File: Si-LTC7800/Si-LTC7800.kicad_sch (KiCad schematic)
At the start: 40 parts, among them Q1 BSC100N06LS3_G, Q2 BSC100N06LS3_G, U1 LTC7800HUDC_PBF

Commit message: power traces sortof done
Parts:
- renumbered R3 to RSENSE
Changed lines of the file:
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@@
 		(on_board yes)
 		(dnp no)
-		(property "Reference" "R3"
+		(property "Reference" "RSENSE"
 			(at 217.17 94.742 90)
 			(effects
@@
 			(project "Si-LTC7800"
 				(path "/1cd71796-7ea7-422d-abea-f4fbd11d4a75"
-					(reference "R3")
+					(reference "RSENSE")
 					(unit 1)
 				)

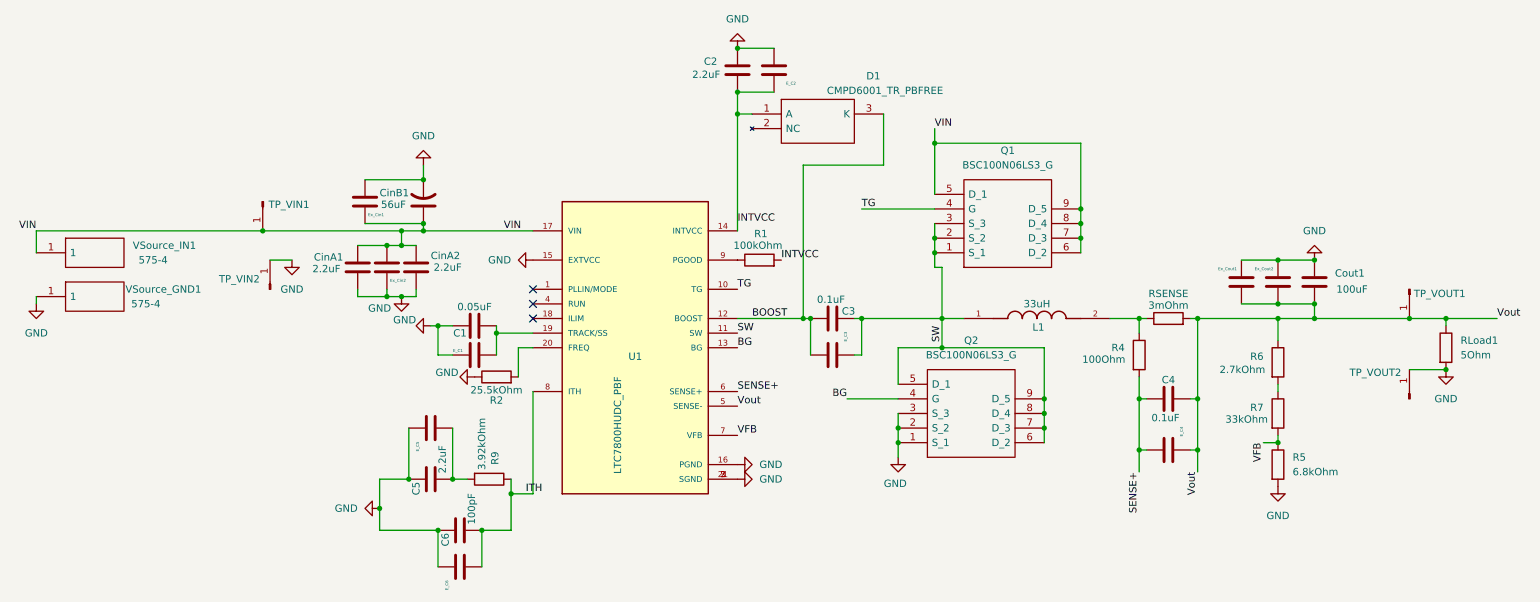
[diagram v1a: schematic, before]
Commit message: Changed font size and names on PCB
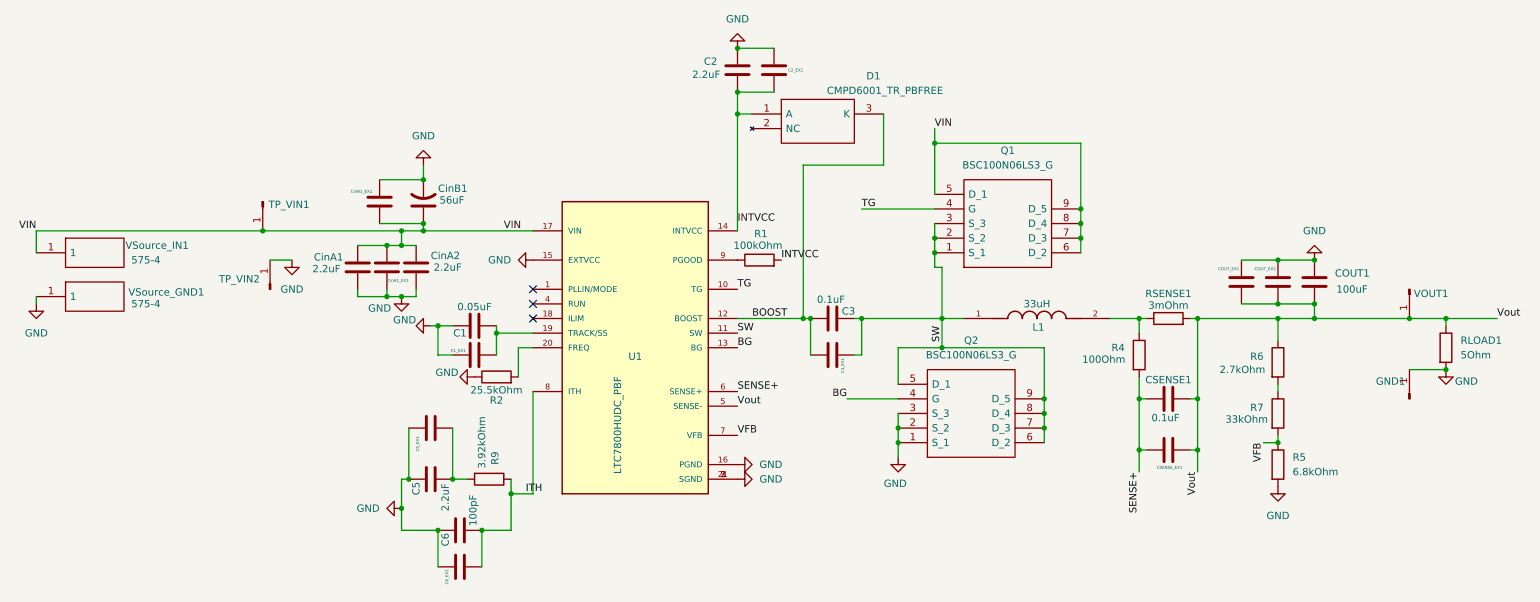
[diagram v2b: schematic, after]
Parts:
- renumbered E_C1 to C1_EX1, E_C2 to C2_EX1, E_C3 to C3_EX1, E_C5 to C5_EX1, E_C6 to C6_EX1, Cout1 to COUT1, Ex_Cout1 to COUT_EX1, Ex_Cout2 to COUT_EX2, C4 to CSENSE1, E_C4 to CSENSE_EX1, Ex_Cin2 to CinA1_EX1, Ex_Cin1 to CinB1_EX1, TP_VOUT2 to GND1, RLoad1 to RLOAD1, RSENSE to RSENSE1, TP_VOUT1 to VOUT1
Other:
- moved on the sheet: CinB1_EX1
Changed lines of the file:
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@@
 	)
 	(junction
-		(at 80.01 132.08)
+		(at 83.82 132.08)
 		(diameter 0)
 		(color 0 0 0 0)
@@
 	(wire
 		(pts
-			(xy 80.01 127) (xy 85.09 127)
+			(xy 83.82 127) (xy 85.09 127)
 		)
 		(stroke
@@
 	(wire
 		(pts
-			(xy 80.01 132.08) (xy 80.01 127)
+			(xy 83.82 132.08) (xy 83.82 127)
 		)
 		(stroke
@@
 	(wire
 		(pts
-			(xy 77.47 74.93) (xy 87.63 74.93)
+			(xy 80.01 74.93) (xy 87.63 74.93)
 		)
 		(stroke
@@
 	(wire
 		(pts
-			(xy 80.01 132.08) (xy 80.01 135.89)
+			(xy 83.82 132.08) (xy 83.82 135.89)
 		)
 		(stroke
@@
 	(wire
 		(pts
-			(xy 80.01 135.89) (xy 90.17 135.89)
+			(xy 83.82 135.89) (xy 90.17 135.89)
 		)
 		(stroke
@@
 	(wire
 		(pts
-			(xy 77.47 82.55) (xy 87.63 82.55)
+			(xy 80.01 82.55) (xy 87.63 82.55)
 		)
 		(stroke
@@
 		(on_board yes)
 		(dnp no)
-		(property "Reference" "E_C5"
+		(property "Reference" "C5_EX1"
 			(at 86.614 122.174 0)
 			(effects
@@
 			(project "Si-LTC7800"
 				(path "/1cd71796-7ea7-422d-abea-f4fbd11d4a75"
-					(reference "E_C5")
+					(reference "C5_EX1")
 					(unit 1)
 				)
@@
 		(on_board yes)
 		(dnp no)
-		(property "Reference" "E_C1"
-			(at 94.488 104.648 90)
+		(property "Reference" "C1_EX1"
+			(at 94.996 104.648 90)
 			(effects
 				(font
@@
 			(project "Si-LTC7800"
 				(path "/1cd71796-7ea7-422d-abea-f4fbd11d4a75"
-					(reference "E_C1")
+					(reference "C1_EX1")
 					(unit 1)
 				)
@@
 		(on_board yes)
 		(dnp no)
-		(property "Reference" "TP_VOUT2"
-			(at 248.666 108.458 90)
+		(property "Reference" "GND1"
+			(at 253.238 109.982 90)
 			(effects
 				(font
@@
 		)
 		(property "Value" "~"
-			(at 248.92 110.744 90)
+			(at 256.032 111.506 90)
 			(effects
 				(font
@@
 			(project "Si-LTC7800"
 				(path "/1cd71796-7ea7-422d-abea-f4fbd11d4a75"
-					(reference "TP_VOUT2")
+					(reference "GND1")
 					(unit 1)
 				)
@@
 		(on_board yes)
 		(dnp no)
-		(property "Reference" "TP_VOUT1"
+		(property "Reference" "VOUT1"
 			(at 259.842 94.742 90)
 			(effects
@@
 			(project "Si-LTC7800"
 				(path "/1cd71796-7ea7-422d-abea-f4fbd11d4a75"
-					(reference "TP_VOUT1")
+					(reference "VOUT1")
 					(unit 1)
 				)
@@
 		(on_board yes)
 		(dnp no)
-		(property "Reference" "Ex_Cin2"
-			(at 84.582 92.456 0)
+		(property "Reference" "CinA1_EX1"
+			(at 85.09 92.456 0)
 			(effects
 				(font
@@
 			(project "Si-LTC7800"
 				(path "/1cd71796-7ea7-422d-abea-f4fbd11d4a75"
-					(reference "Ex_Cin2")
+					(reference "CinA1_EX1")
 					(unit 1)
 				)
@@
 		(on_board yes)
 		(dnp no)
-		(property "Reference" "RSENSE"
+		(property "Reference" "RSENSE1"
 			(at 217.17 94.742 90)
 			(effects
@@
 			(project "Si-LTC7800"
 				(path "/1cd71796-7ea7-422d-abea-f4fbd11d4a75"
-					(reference "RSENSE")
+					(reference "RSENSE1")
 					(unit 1)
 				)
@@
 		(on_board yes)
 		(dnp no)
-		(property "Reference" "Cout1"
+		(property "Reference" "COUT1"
 			(at 246.126 91.186 0)
 			(effects
@@
 			(project "Si-LTC7800"
 				(path "/1cd71796-7ea7-422d-abea-f4fbd11d4a75"
-					(reference "Cout1")
+					(reference "COUT1")
 					(unit 1)
 				)
@@
 		(on_board yes)
 		(dnp no)
-		(property "Reference" "E_C2"
-			(at 152.4 58.166 0)
+		(property "Reference" "C2_EX1"
+			(at 153.67 55.88 0)
 			(effects
 				(font
@@
 		)
 		(property "Value" "~"
-			(at 150.368 57.404 0)
+			(at 152.908 56.642 0)
 			(effects
 				(font
@@
 			(project "Si-LTC7800"
 				(path "/1cd71796-7ea7-422d-abea-f4fbd11d4a75"
-					(reference "E_C2")
+					(reference "C2_EX1")
 					(unit 1)
 				)
@@
 		(on_board yes)
 		(dnp no)
-		(property "Reference" "E_C4"
-			(at 219.456 117.856 0)
+		(property "Reference" "CSENSE_EX1"
+			(at 215.138 124.968 90)
 			(effects
 				(font
@@
 			(project "Si-LTC7800"
 				(path "/1cd71796-7ea7-422d-abea-f4fbd11d4a75"
-					(reference "E_C4")
+					(reference "CSENSE_EX1")
 					(unit 1)
 				)
@@
 		)
 		(property "Value" "100pF"
-			(at 96.012 134.874 0)
+			(at 96.266 135.128 0)
 			(effects
 				(font
@@
 		(dnp no)
 		(property "Reference" "CinB1"
-			(at 80.01 77.216 0)
+			(at 90.17 76.454 0)
 			(effects
 				(font
@@
 		)
 		(property "Value" "56uF"
-			(at 80.264 79.248 0)
+			(at 90.424 78.486 0)
 			(effects
 				(font
@@
 		(dnp no)
 		(fields_autoplaced yes)
-		(property "Reference" "RLoad1"
+		(property "Reference" "RLOAD1"
 			(at 267.97 102.8699 0)
 			(effects
@@
 			(project ""
 				(path "/1cd71796-7ea7-422d-abea-f4fbd11d4a75"
-					(reference "RLoad1")
+					(reference "RLOAD1")
 					(unit 1)
 				)
@@
 		(on_board yes)
 		(dnp no)
-		(property "Reference" "Ex_Cout1"
+		(property "Reference" "COUT_EX1"
 			(at 225.806 90.424 0)
 			(effects
@@
 			(project "Si-LTC7800"
 				(path "/1cd71796-7ea7-422d-abea-f4fbd11d4a75"
-					(reference "Ex_Cout1")
+					(reference "COUT_EX1")
 					(unit 1)
 				)
@@
 	(symbol
 		(lib_id "power:GND")
-		(at 80.01 132.08 270)
+		(at 83.82 132.08 270)
 		(unit 1)
 		(exclude_from_sim no)
@@
 		(fields_autoplaced yes)
 		(property "Reference" "#PWR014"
-			(at 73.66 132.08 0)
+			(at 77.47 132.08 0)
 			(effects
 				(font
@@
 		)
 		(property "Value" "GND"
-			(at 76.2 132.0799 90)
+			(at 80.01 132.0799 90)
 			(effects
 				(font
@@
 		)
 		(property "Footprint" ""
-			(at 80.01 132.08 0)
+			(at 83.82 132.08 0)
 			(effects
 				(font
@@
 		)
 		(property "Datasheet" ""
-			(at 80.01 132.08 0)
+			(at 83.82 132.08 0)
 			(effects
 				(font
@@
 		)
 		(property "Description" "Power symbol creates a global label with name \"GND\" , ground"
-			(at 80.01 132.08 0)
+			(at 83.82 132.08 0)
 			(effects
 				(font
@@
 		(on_board yes)
 		(dnp no)
-		(property "Reference" "E_C6"
-			(at 91.694 146.304 0)
+		(property "Reference" "C6_EX1"
+			(at 91.694 145.288 0)
 			(effects
 				(font
@@
 			(project "Si-LTC7800"
 				(path "/1cd71796-7ea7-422d-abea-f4fbd11d4a75"
-					(reference "E_C6")
+					(reference "C6_EX1")
 					(unit 1)
 				)
@@
 		)
 		(property "Value" "2.2uF"
-			(at 90.932 125.984 0)
+			(at 91.44 132.588 0)
 			(effects
 				(font
@@
 		)
 		(property "Value" "3.92kOhm"
-			(at 97.79 116.332 0)
+			(at 97.79 116.078 0)
 			(effects
 				(font
@@
 		(on_board yes)
 		(dnp no)
-		(property "Reference" "E_C3"
-			(at 161.036 101.346 0)
+		(property "Reference" "C3_EX1"
+			(at 160.528 105.918 0)
 			(effects
 				(font
@@
 		)
 		(property "Value" "~"
-			(at 160.274 103.632 0)
+			(at 161.29 106.934 0)
 			(effects
 				(font
@@
 			(project "Si-LTC7800"
 				(path "/1cd71796-7ea7-422d-abea-f4fbd11d4a75"
-					(reference "E_C3")
+					(reference "C3_EX1")
 					(unit 1)
 				)
@@
 	(symbol
 		(lib_id "Device:C")
-		(at 77.47 78.74 180)
+		(at 80.01 78.74 180)
 		(unit 1)
 		(exclude_from_sim no)
@@
 		(on_board yes)
 		(dnp no)
-		(property "Reference" "Ex_Cin1"
-			(at 80.772 81.026 0)
+		(property "Reference" "CinB1_EX1"
+			(at 78.74 76.962 0)
 			(effects
 				(font
@@
 		)
 		(property "Value" "~"
-			(at 79.248 80.264 0)
+			(at 81.788 80.264 0)
 			(effects
 				(font
@@
 		)
 		(property "Footprint" "Capacitor_SMD:C_0805_2012Metric_Pad1.18x1.45mm_HandSolder"
-			(at 76.5048 74.93 0)
+			(at 79.0448 74.93 0)
 			(effects
 				(font
@@
 		)
 		(property "Datasheet" "~"
-			(at 77.47 78.74 0)
+			(at 80.01 78.74 0)
 			(effects
 				(font
@@
 		)
 		(property "Description" "Unpolarized capacitor"
-			(at 77.47 78.74 0)
+			(at 80.01 78.74 0)
 			(effects
 				(font
@@
 			(project "Si-LTC7800"
 				(path "/1cd71796-7ea7-422d-abea-f4fbd11d4a75"
-					(reference "Ex_Cin1")
+					(reference "CinB1_EX1")
 					(unit 1)
 				)
@@
 		(dnp no)
 		(property "Reference" "VSource_GND1"
-			(at 35.814 93.98 0)
+			(at 36.322 94.488 0)
 			(effects
 				(font
@@
 		(dnp no)
 		(property "Reference" "VSource_IN1"
-			(at 37.084 86.36 0)
+			(at 35.814 86.36 0)
 			(effects
 				(font
@@
 		)
 		(property "Value" "575-4"
-			(at 38.1 88.8999 0)
+			(at 36.83 88.8999 0)
 			(effects
 				(font
@@
 		(on_board yes)
 		(dnp no)
-		(property "Reference" "Ex_Cout2"
+		(property "Reference" "COUT_EX2"
 			(at 232.156 90.424 0)
 			(effects
@@
 			(project "Si-LTC7800"
 				(path "/1cd71796-7ea7-422d-abea-f4fbd11d4a75"
-					(reference "Ex_Cout2")
+					(reference "COUT_EX2")
 					(unit 1)
 				)
@@
 		(on_board yes)
 		(dnp no)
-		(fields_autoplaced yes)
 		(property "Reference" "#PWR03"
 			(at 265.43 114.3 0)
@@
 		)
 		(property "Value" "GND"
-			(at 265.43 113.03 0)
+			(at 268.986 109.982 0)
 			(effects
 				(font
@@
 		(on_board yes)
 		(dnp no)
-		(property "Reference" "C4"
+		(property "Reference" "CSENSE1"
 			(at 217.17 109.728 90)
 			(effects
@@
 			(project "Si-LTC7800"
 				(path "/1cd71796-7ea7-422d-abea-f4fbd11d4a75"
-					(reference "C4")
+					(reference "CSENSE1")
 					(unit 1)
 				)

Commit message: GaN PCB update
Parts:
- Q1, Q2: footprint XT60PW-M:BSC100N06LS3G -> Transistor_Power:BSC100N06LS3G
- U1: footprint Package_DFN_QFN:QFN50P400X300X80-21N -> Library:QFN50P400X300X80-21N
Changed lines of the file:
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@@
 			)
 		)
-		(property "Footprint" "XT60PW-M:BSC100N06LS3G"
+		(property "Footprint" "Transistor_Power:BSC100N06LS3G"
 			(at 198.12 90.17 0)
 			(effects
@@
 			)
 		)
-		(property "Footprint" "Package_DFN_QFN:QFN50P400X300X80-21N"
+		(property "Footprint" "Library:QFN50P400X300X80-21N"
 			(at 129.032 104.902 90)
 			(effects
@@
 			)
 		)
-		(property "Footprint" "XT60PW-M:BSC100N06LS3G"
+		(property "Footprint" "Transistor_Power:BSC100N06LS3G"
 			(at 191.77 123.19 0)
 			(effects

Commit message: Updating PCBs for preassembly
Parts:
- added RLOAD2: 2Ohm, Resistor_SMD:R_0201_0603Metric, symbol Device:R
- C1, C3, CSENSE1: footprint Capacitor_SMD:C_0805_2012Metric_Pad1.18x1.45mm_HandSolder -> Capacitor_SMD:C_0805_2012Metric; LCSC (none) -> C49678
- C2, C5, CinA1, CinA2: footprint Capacitor_SMD:C_0805_2012Metric_Pad1.18x1.45mm_HandSolder -> Capacitor_SMD:C_0805_2012Metric; LCSC (none) -> C19110
- C6: footprint Capacitor_SMD:C_0805_2012Metric_Pad1.18x1.45mm_HandSolder -> Capacitor_SMD:C_0805_2012Metric; LCSC (none) -> C1970
- COUT1: footprint Capacitor_SMD:C_0805_2012Metric_Pad1.18x1.45mm_HandSolder -> Capacitor_SMD:C_0805_2012Metric; LCSC (none) -> C141660
- CinB1: footprint Capacitor_SMD:C_0805_2012Metric_Pad1.18x1.45mm_HandSolder -> Capacitor_Tantalum_SMD:CP_EIA-7343-31_Kemet-D; LCSC (none) -> C465937
- D1: LCSC (none) -> C17357273
- Q1, Q2: LCSC (none) -> C72767
- R1: footprint Resistor_SMD:R_0201_0603Metric_Pad0.64x0.40mm_HandSolder -> Resistor_SMD:R_0201_0603Metric; LCSC (none) -> C14675
- R2: footprint Resistor_SMD:R_0201_0603Metric_Pad0.64x0.40mm_HandSolder -> Resistor_SMD:R_0201_0603Metric; LCSC (none) -> C861257
- R4: footprint Resistor_SMD:R_0201_0603Metric_Pad0.64x0.40mm_HandSolder -> Resistor_SMD:R_0201_0603Metric; LCSC (none) -> C105588
- R5: footprint Resistor_SMD:R_0201_0603Metric_Pad0.64x0.40mm_HandSolder -> Resistor_SMD:R_0201_0603Metric; LCSC (none) -> C2907055
- R6: footprint Resistor_SMD:R_0201_0603Metric_Pad0.64x0.40mm_HandSolder -> Resistor_SMD:R_0201_0603Metric; LCSC (none) -> C2907008
- R7: footprint Resistor_SMD:R_0201_0603Metric_Pad0.64x0.40mm_HandSolder -> Resistor_SMD:R_0201_0603Metric; LCSC (none) -> C2907028
- R9: footprint Resistor_SMD:R_0201_0603Metric_Pad0.64x0.40mm_HandSolder -> Resistor_SMD:R_0201_0603Metric; LCSC (none) -> C4168160
- RLOAD1: value 5Ohm -> 3Ohm; footprint Resistor_SMD:R_0201_0603Metric_Pad0.64x0.40mm_HandSolder -> Resistor_SMD:R_0201_0603Metric; LCSC (none) -> C23157
- RSENSE1: footprint Resistor_SMD:R_0201_0603Metric_Pad0.64x0.40mm_HandSolder -> Resistor_SMD:R_0201_0603Metric; LCSC (none) -> C7256520
- U1: LCSC (none) -> C690192
- VSource_GND1, VSource_IN1: LCSC (none) -> C4944061
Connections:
- net GND: now also RLOAD2.2; no longer RLOAD1.2
- new net: RLOAD1.2, RLOAD2.1
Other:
- moved on the sheet: GND1
